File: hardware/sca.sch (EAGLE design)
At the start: 30 parts

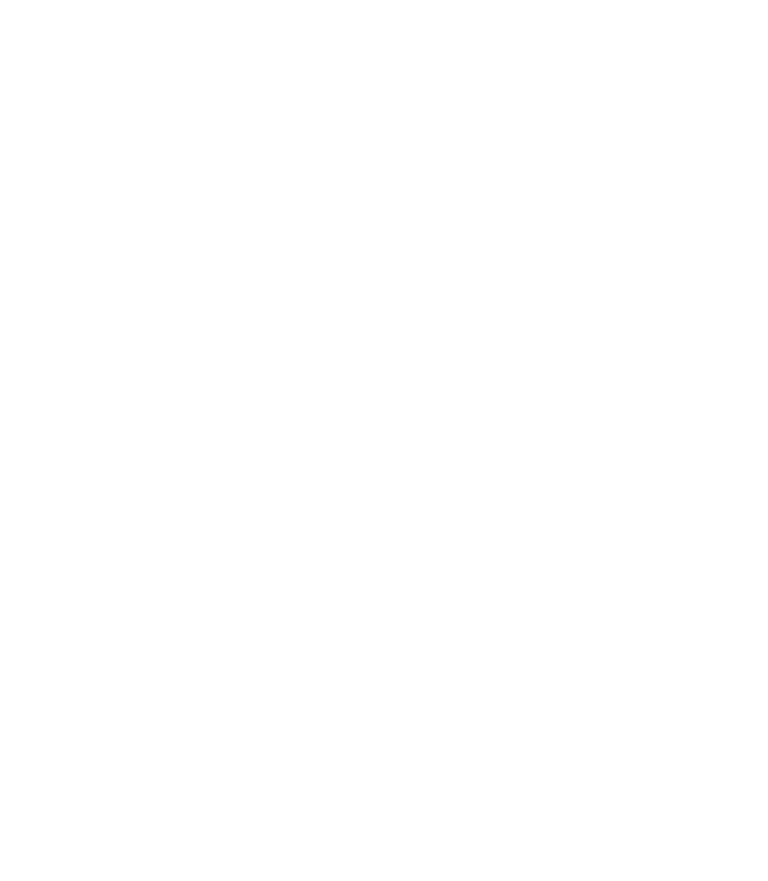
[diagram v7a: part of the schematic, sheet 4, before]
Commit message: Added Decoupling Caps for Xbee per datasheet
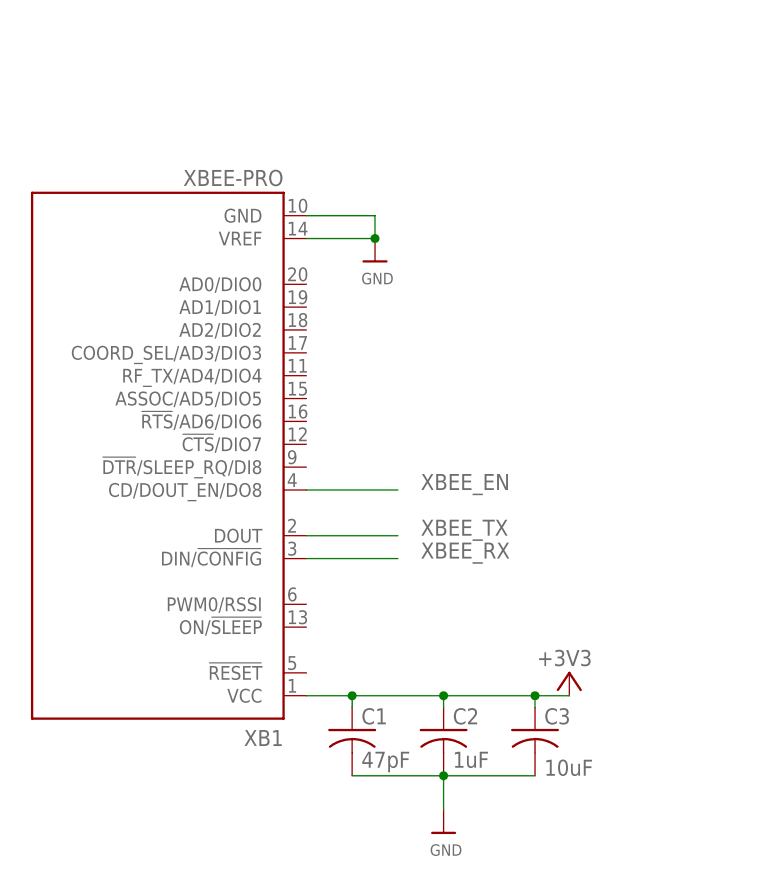
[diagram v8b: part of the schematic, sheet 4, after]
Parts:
- added C1: 47pF, adafruit:C-US025-040X050
- added C2: 1uF, adafruit:C-US025-040X050
- added C3: 10uF, adafruit:C-US025-040X050
- added XB1: XBEE-PRO, maxstream:XBEE-PRO
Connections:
- new net XBEE_EN: U$9.28, XB1.CD/DOUT_EN/DO8
- net +3V3: now also C1.1, C2.1, C3.1, XB1.VCC
- net GND: now also C1.2, C2.2, C3.2, XB1.GND, XB1.VREF
- net XBEE_RX: now also XB1.DIN/!CONFIG
- net XBEE_TX: now also XB1.DOUT
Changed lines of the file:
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@@
 <schematic_group name="5V_REGULATOR"/>
 <schematic_group name="GPS"/>
+<schematic_group name="XBEE"/>
 <schematic_group name="LED_BANK1"/>
 <schematic_group name="BATTERY_VOLTAGE1"/>
@@
 </groups>
 <parts>
+<part name="XB1" library="maxstream" library_urn="urn:adsk.eagle:library:270" deviceset="XBEE" device="-PRO" package3d_urn="urn:adsk.eagle:package:18008/1"/>
 <part name="5V_REG" library="adafruit" library_urn="urn:adsk.eagle:library:420" deviceset="78*" device="T" package3d_urn="urn:adsk.eagle:package:6240670/1" technology="12"/>
 <part name="3V3_REG" library="adafruit" library_urn="urn:adsk.eagle:library:420" deviceset="78*" device="T" package3d_urn="urn:adsk.eagle:package:6240670/1" technology="12"/>
@@
 <part name="+3V2" library="supply1" deviceset="+3V3" device=""/>
 <part name="P+3" library="supply1" deviceset="+5V" device=""/>
+<part name="U$28" library="microbuilder" deviceset="GND" device=""/>
 <part name="PH1" library="photo-elements" library_urn="urn:adsk.eagle:library:323" deviceset="A10" device="" package3d_urn="urn:adsk.eagle:package:22201/1" technology="50_09"/>
 <part name="U$30" library="microbuilder" deviceset="GND" device=""/>
@@
 <part name="PH4" library="photo-elements" library_urn="urn:adsk.eagle:library:323" deviceset="A10" device="" package3d_urn="urn:adsk.eagle:package:22201/1" technology="50_09"/>
 <part name="U$33" library="microbuilder" deviceset="GND" device=""/>
+<part name="+3V4" library="supply1" deviceset="+3V3" device=""/>
 <part name="R20" library="varistor" library_urn="urn:adsk.eagle:library:410" deviceset="THERMISTOR" device="-2,5" package3d_urn="urn:adsk.eagle:package:30592/1"/>
 <part name="U$59" library="microbuilder" deviceset="GND" device=""/>
@@
 <part name="FRAME3" library="frames" library_urn="urn:adsk.eagle:library:229" deviceset="A4L-LOC" device=""/>
 <part name="FRAME4" library="frames" library_urn="urn:adsk.eagle:library:229" deviceset="A4L-LOC" device=""/>
+<part name="C1" library="adafruit" library_urn="urn:adsk.eagle:library:420" deviceset="C-US" device="025-040X050" package3d_urn="urn:adsk.eagle:package:6240321/1" value="47pF"/>
+<part name="C2" library="adafruit" library_urn="urn:adsk.eagle:library:420" deviceset="C-US" device="025-040X050" package3d_urn="urn:adsk.eagle:package:6240321/1" value="1uF"/>
+<part name="C3" library="adafruit" library_urn="urn:adsk.eagle:library:420" deviceset="C-US" device="025-040X050" package3d_urn="urn:adsk.eagle:package:6240321/1" value="10uF"/>
+<part name="U$12" library="microbuilder" deviceset="GND" device=""/>
 </parts>
 <sheets>
@@
 </segment>
 </net>
+<net name="XBEE_EN" class="0">
+<segment>
+<pinref part="U$9" gate="G$1" pin="28"/>
+<wire x1="109.22" y1="71.12" x2="99.06" y2="71.12" width="0.1524" layer="91"/>
+<label x="86.36" y="71.12" size="1.778" layer="95"/>
+</segment>
+</net>
 </nets>
 </sheet>
@@
 <attribute name="VALUE" x="134.62" y="95.25" size="1.778" layer="96" rot="R180"/>
 </instance>
+<instance part="XB1" gate="G$1" x="53.34" y="93.98" smashed="yes" rot="R180" grouprefs="XBEE">
+<attribute name="NAME" x="66.04" y="64.77" size="1.778" layer="95" rot="R180"/>
+<attribute name="VALUE" x="66.04" y="127" size="1.778" layer="96" rot="R180"/>
+</instance>
+<instance part="U$28" gate="G$1" x="76.2" y="116.84" smashed="yes" grouprefs="XBEE">
+<attribute name="VALUE" x="74.676" y="114.3" size="1.27" layer="96"/>
+</instance>
+<instance part="+3V4" gate="G$1" x="97.79" y="71.12" smashed="yes" grouprefs="XBEE">
+<attribute name="VALUE" x="100.33" y="73.66" size="1.778" layer="96" rot="R180"/>
+</instance>
+<instance part="C1" gate="G$1" x="73.66" y="64.77" smashed="yes" grouprefs="XBEE">
+<attribute name="NAME" x="74.676" y="65.405" size="1.778" layer="95"/>
+<attribute name="VALUE" x="74.676" y="60.579" size="1.778" layer="96"/>
+</instance>
+<instance part="C2" gate="G$1" x="83.82" y="64.77" smashed="yes" grouprefs="XBEE">
+<attribute name="NAME" x="84.836" y="65.405" size="1.778" layer="95"/>
+<attribute name="VALUE" x="84.836" y="60.579" size="1.778" layer="96"/>
+</instance>
+<instance part="C3" gate="G$1" x="93.98" y="64.77" smashed="yes" grouprefs="XBEE">
+<attribute name="NAME" x="94.996" y="65.405" size="1.778" layer="95"/>
+<attribute name="VALUE" x="94.996" y="60.579" size="1.778" layer="96" align="center-left"/>
+</instance>
+<instance part="U$12" gate="G$1" x="83.82" y="53.34" smashed="yes" grouprefs="XBEE">
+<attribute name="VALUE" x="82.296" y="50.8" size="1.27" layer="96"/>
+</instance>
 </instances>
 <busses>
@@
 <pinref part="JP4" gate="A" pin="3"/>
 </segment>
+<segment>
+<pinref part="XB1" gate="G$1" pin="GND"/>
+<wire x1="68.58" y1="121.92" x2="76.2" y2="121.92" width="0.1524" layer="91" grouprefs="XBEE"/>
+<pinref part="U$28" gate="G$1" pin="GND"/>
+<wire x1="76.2" y1="121.92" x2="76.2" y2="119.38" width="0.1524" layer="91" grouprefs="XBEE"/>
+<pinref part="XB1" gate="G$1" pin="VREF"/>
+<wire x1="68.58" y1="119.38" x2="76.2" y2="119.38" width="0.1524" layer="91" grouprefs="XBEE"/>
+<junction x="76.2" y="119.38" grouprefs="XBEE"/>
+</segment>
+<segment>
+<pinref part="C1" gate="G$1" pin="2"/>
+<pinref part="C2" gate="G$1" pin="2"/>
+<wire x1="73.66" y1="59.69" x2="83.82" y2="59.69" width="0.1524" layer="91" grouprefs="XBEE"/>
+<pinref part="C3" gate="G$1" pin="2"/>
+<wire x1="93.98" y1="59.69" x2="83.82" y2="59.69" width="0.1524" layer="91" grouprefs="XBEE"/>
+<junction x="83.82" y="59.69" grouprefs="XBEE"/>
+<pinref part="U$12" gate="G$1" pin="GND"/>
+<wire x1="83.82" y1="55.88" x2="83.82" y2="59.69" width="0.1524" layer="91" grouprefs="XBEE"/>
+</segment>
 </net>
 <net name="PS1_3V" class="0">
@@
 <wire x1="214.63" y1="96.52" x2="214.63" y2="91.44" width="0.1524" layer="91" grouprefs="BMP338"/>
 </segment>
+<segment>
+<pinref part="XB1" gate="G$1" pin="VCC"/>
+<wire x1="68.58" y1="68.58" x2="73.66" y2="68.58" width="0.1524" layer="91" grouprefs="XBEE"/>
+<pinref part="+3V4" gate="G$1" pin="+3V3"/>
+<pinref part="C1" gate="G$1" pin="1"/>
+<wire x1="73.66" y1="68.58" x2="83.82" y2="68.58" width="0.1524" layer="91" grouprefs="XBEE"/>
+<wire x1="83.82" y1="68.58" x2="93.98" y2="68.58" width="0.1524" layer="91" grouprefs="XBEE"/>
+<wire x1="93.98" y1="68.58" x2="97.79" y2="68.58" width="0.1524" layer="91" grouprefs="XBEE"/>
+<wire x1="73.66" y1="67.31" x2="73.66" y2="68.58" width="0.1524" layer="91" grouprefs="XBEE"/>
+<junction x="73.66" y="68.58" grouprefs="XBEE"/>
+<pinref part="C2" gate="G$1" pin="1"/>
+<wire x1="83.82" y1="67.31" x2="83.82" y2="68.58" width="0.1524" layer="91" grouprefs="XBEE"/>
+<junction x="83.82" y="68.58" grouprefs="XBEE"/>
+<pinref part="C3" gate="G$1" pin="1"/>
+<wire x1="93.98" y1="67.31" x2="93.98" y2="68.58" width="0.1524" layer="91" grouprefs="XBEE"/>
+<junction x="93.98" y="68.58" grouprefs="XBEE"/>
+</segment>
 </net>
 <net name="+5V" class="0">
@@
 </segment>
 </net>
+<net name="XBEE_RX" class="0">
+<segment>
+<pinref part="XB1" gate="G$1" pin="DIN/!CONFIG"/>
+<wire x1="68.58" y1="83.82" x2="78.74" y2="83.82" width="0.1524" layer="91" grouprefs="XBEE"/>
+<label x="81.28" y="83.82" size="1.778" layer="95" grouprefs="XBEE"/>
+</segment>
+</net>
+<net name="XBEE_TX" class="0">
+<segment>
+<pinref part="XB1" gate="G$1" pin="DOUT"/>
+<wire x1="68.58" y1="86.36" x2="78.74" y2="86.36" width="0.1524" layer="91" grouprefs="XBEE"/>
+<label x="81.28" y="86.36" size="1.778" layer="95" grouprefs="XBEE"/>
+</segment>
+</net>
+<net name="XBEE_EN" class="0">
+<segment>
+<pinref part="XB1" gate="G$1" pin="CD/DOUT_EN/DO8"/>
+<wire x1="68.58" y1="91.44" x2="78.74" y2="91.44" width="0.1524" layer="91"/>
+<label x="81.28" y="91.44" size="1.778" layer="95"/>
+</segment>
+</net>
